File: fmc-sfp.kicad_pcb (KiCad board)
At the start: 2 copper layers, 89.5 x 70 mm, 35 parts, among them J1 ASP-134604-01, J2 SFP+, J3 SFP+, J4 132134, J5 132134, J6 132134, J7 132134, SW1 CHS-02TB, U1 MAX9113EKA_TT, U2 MAX9113EKA_TT

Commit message: clean up schematic and pcb
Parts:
- moved R10 0.52 mm to (71.0, 64.4)
- moved R9 0.52 mm to (71.0, 62.5)
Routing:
- net +3V3: track 122.4 -> 116.8 mm
- net GND: track 22.4 -> 25.1 mm, vias 10 -> 9
- net /lvds_0_rx_N: track 33.1 -> 34.9 mm
- net /lvds_1_tx_N: track 48.6 -> 50.2 mm
- net /lvds_0_tx_N: track 36.3 -> 35.1 mm
- net /FMC_LA02_N: track 5.20 -> 6.37 mm
- net /FMC_LA02_P: track 5.20 -> 6.35 mm
- net /lvds_0_tx_P: track 37.0 -> 37.7 mm
- net /lvds_1_tx_P: track 49.6 -> 50.3 mm
- net /lvds_0_rx_P: track 33.2 -> 32.6 mm

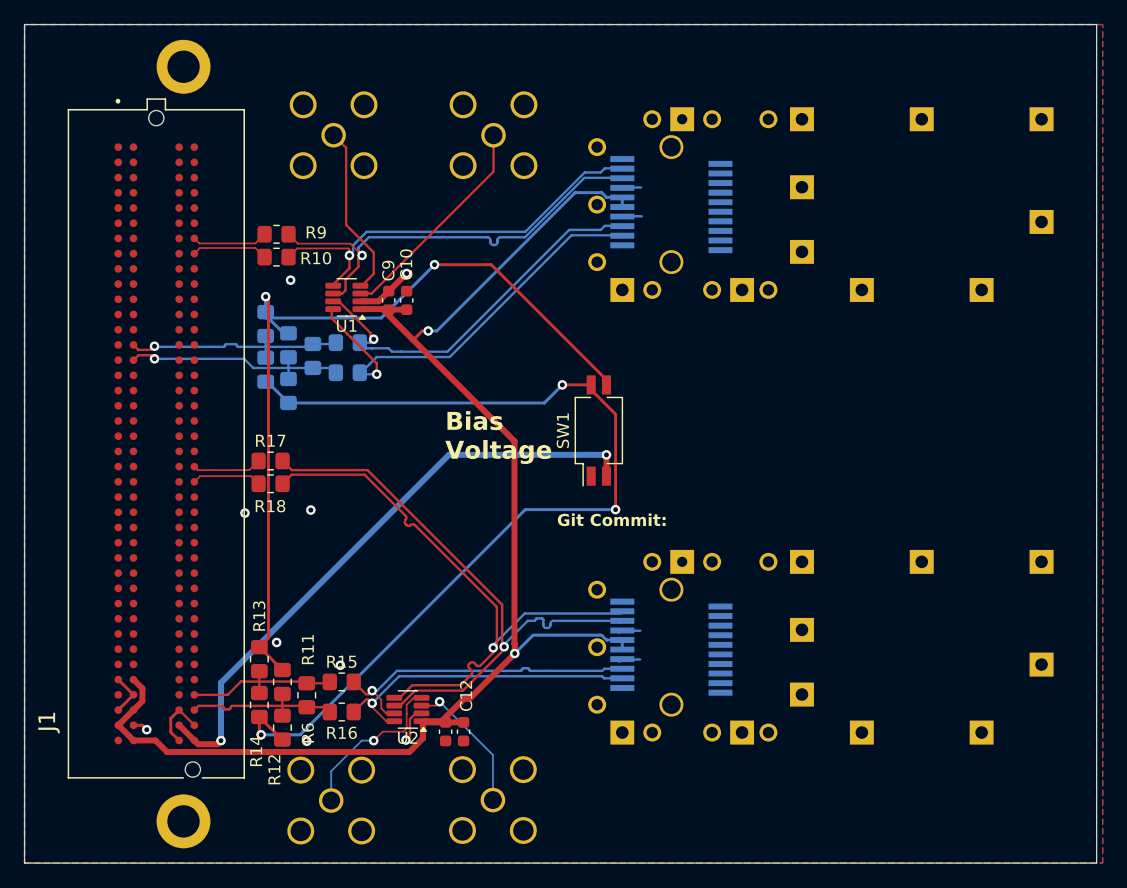
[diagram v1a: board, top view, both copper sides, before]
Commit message: make board more symetrical
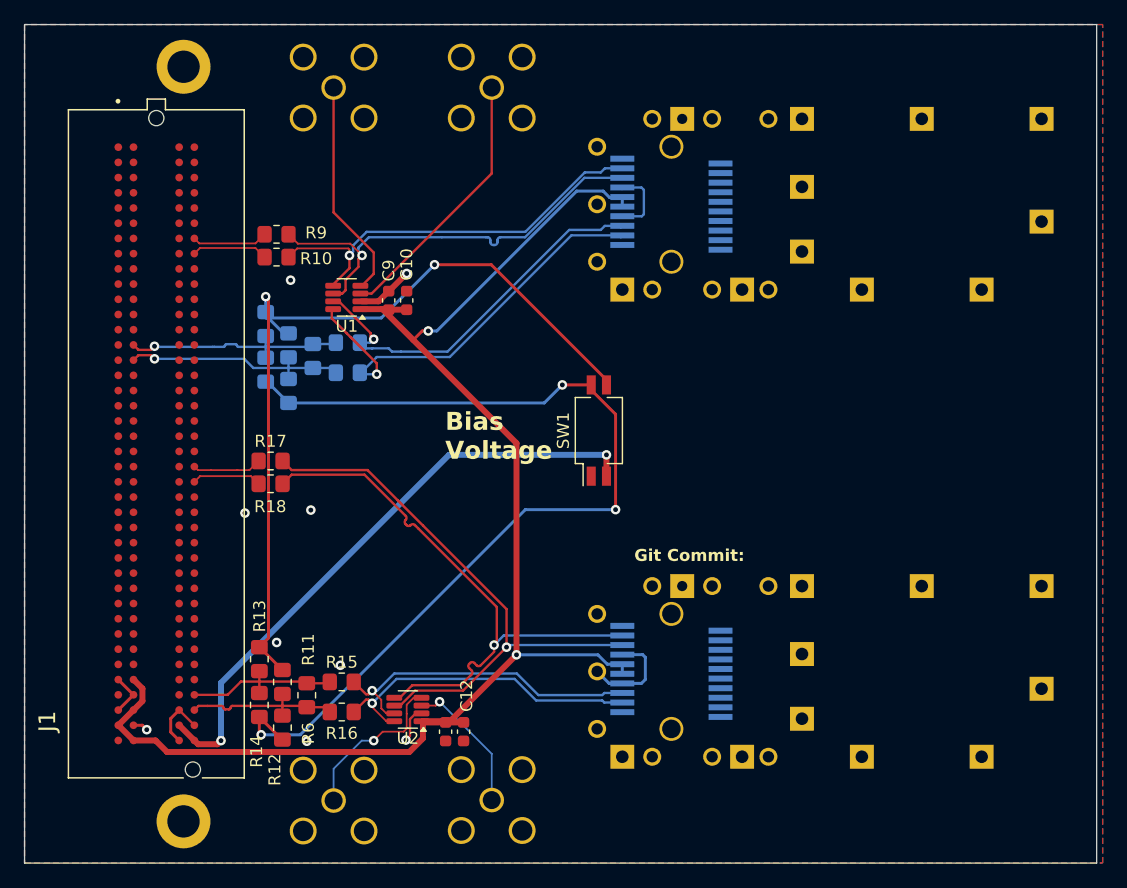
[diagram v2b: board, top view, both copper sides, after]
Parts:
- moved J4 3.98 mm to (89.0, 50.3)
- moved J5 3.98 mm to (75.8, 50.3)
- moved J2 2.02 mm to (97.8, 99.0)
- moved J6 0.20 mm to (75.8, 109.8)
- moved J7 0.10 mm to (89.0, 109.7)
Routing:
- net GND: track 25.1 -> 32.4 mm
- net /TX0: track 14.4 -> 18.3 mm
- net /RX0: track 18.2 -> 22.0 mm
- net /lvds_1_tx_P: track 50.3 -> 48.2 mm
- net /TX1: track 12.6 -> 13.6 mm
- net /lvds_1_tx_N: track 50.2 -> 49.3 mm
- net /lvds_1_rx_N: track 26.6 -> 27.3 mm

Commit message: add single x4 switch and test pads for differential probing
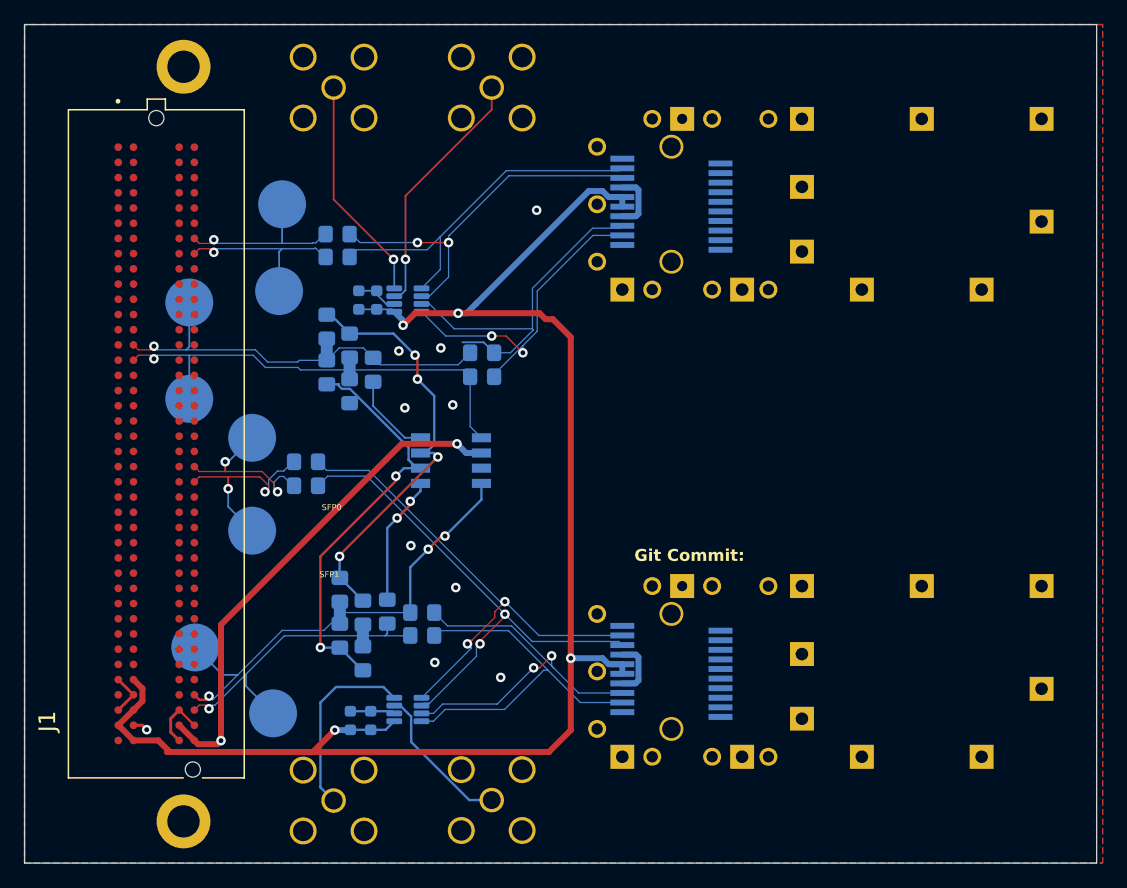
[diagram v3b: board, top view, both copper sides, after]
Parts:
- added TP1: SFP0 RX+, TestPoint:TestPoint_Pad_D4.0mm, B.Cu at (63.8, 68.2)
- added TP2: SFP0 RX-, TestPoint:TestPoint_Pad_D4.0mm, B.Cu at (63.8, 76.2)
- added TP3: SFP0 TX+, TestPoint:TestPoint_Pad_D4.0mm, B.Cu at (71.5, 60.0)
- added TP4: SFP0 TX-, TestPoint:TestPoint_Pad_D4.0mm, B.Cu at (71.2, 67.2)
- added TP5: SFP1 RX+, TestPoint:TestPoint_Pad_D4.0mm, B.Cu at (69.0, 79.5)
- added TP6: SFP1 RX-, TestPoint:TestPoint_Pad_D4.0mm, B.Cu at (69.0, 87.2)
- added TP7: SFP1 TX+, TestPoint:TestPoint_Pad_D4.0mm, B.Cu at (64.2, 97.0)
- added TP8: SFP1 TX-, TestPoint:TestPoint_Pad_D4.0mm, B.Cu at (70.8, 102.5)
- C10, C11, C12, C9, R10, R11, R12, R13, R14, R15, R16, R17, R18, R6, R9, U1, U2: moved to B.Cu
- SW1: value CHS-02TB -> SW_DIP_x04; footprint Button_Switch_SMD:SW_DIP_SPSTx02_Slide_Copal_CHS-02B_W7.62mm_P1.27mm -> Button_Switch_SMD:SW_DIP_SPSTx04_Slide_Copal_CHS-04A_W5.08mm_P1.27mm_JPin; moved to B.Cu
- moved SW1 12.6 mm to (85.6, 81.4), turned to 180 degrees
- moved R7 11.2 mm to (88.2, 72.4)
- moved R8 11.2 mm to (88.2, 74.4)
- moved R6 9.69 mm to (80.3, 94.0), turned to -90 degrees
- moved C12 9.50 mm to (77.2, 103.1), turned to 90 degrees
- moved R16 9.27 mm to (83.2, 96.0)
- moved R14 8.87 mm to (76.3, 96.0)
- moved R11 8.87 mm to (78.2, 94.1)
- moved R12 8.87 mm to (78.2, 97.9)
- moved R13 8.87 mm to (76.3, 92.2)
- moved R15 8.87 mm to (83.2, 94.1)
- moved C11 6.32 mm to (78.9, 103.1), turned to 90 degrees
- moved R1 5.16 mm to (79.1, 73.8)
- moved R2 5.10 mm to (75.2, 70.2)
- moved R3 5.10 mm to (75.2, 74.0)
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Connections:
- R1 pad 1: /FMC_LA09_N -> Net-(R1-Pad1)
- R6 pad 1: /FMC_LA32_N -> Net-(R6-Pad1)
- R6 pad 2: /FMC_LA32_P -> /FMC_LA32_N
- SW1 pad 1: GND -> /FMC_LA09_N
- SW1 pad 3: /bias_hi -> GND
- SW1 pad 4: /bias_lo -> /FMC_LA32_P
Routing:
- net /bias_lo: track 81.4 -> 35.3 mm, vias 3 -> 2
- net /bias_hi: track 70.4 -> 36.1 mm, vias 2 -> 4
- net /FMC_LA32_P: track 13.9 -> 41.2 mm, vias 0 -> 3
- net /FMC_LA09_N: track 19.5 -> 40.2 mm
- net /FMC_LA09_P: track 19.4 -> 36.3 mm
- net /FMC_LA32_N: track 13.7 -> 28.2 mm, vias 0 -> 1
- net +3V3: track 116.6 -> 129.4 mm, vias 2 -> 4
- net Net-(R6-Pad1): track 0.00 -> 10.9 mm, vias 0 -> 2
- net /FMC_LA19_N: track 5.82 -> 16.5 mm, vias 0 -> 2
- net /FMC_LA19_P: track 5.80 -> 15.1 mm, vias 0 -> 2
- net /FMC_LA02_N: track 6.37 -> 15.3 mm, vias 0 -> 1
- net VADJ: track 50.9 -> 42.3 mm
- net /FMC_LA02_P: track 6.35 -> 15.0 mm, vias 0 -> 1
- net Net-(R1-Pad1): track 0.00 -> 7.09 mm
- net /lvds_0_rx_N: track 34.9 -> 28.1 mm, vias 1 -> 2
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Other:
- board text added: "SW1: 1. Termination SFP0 2. Bias Voltage High 3. Bias Voltage Low 4. Termination SFP1"
- board text removed: "Bias Voltage"

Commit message: fix DRC issues
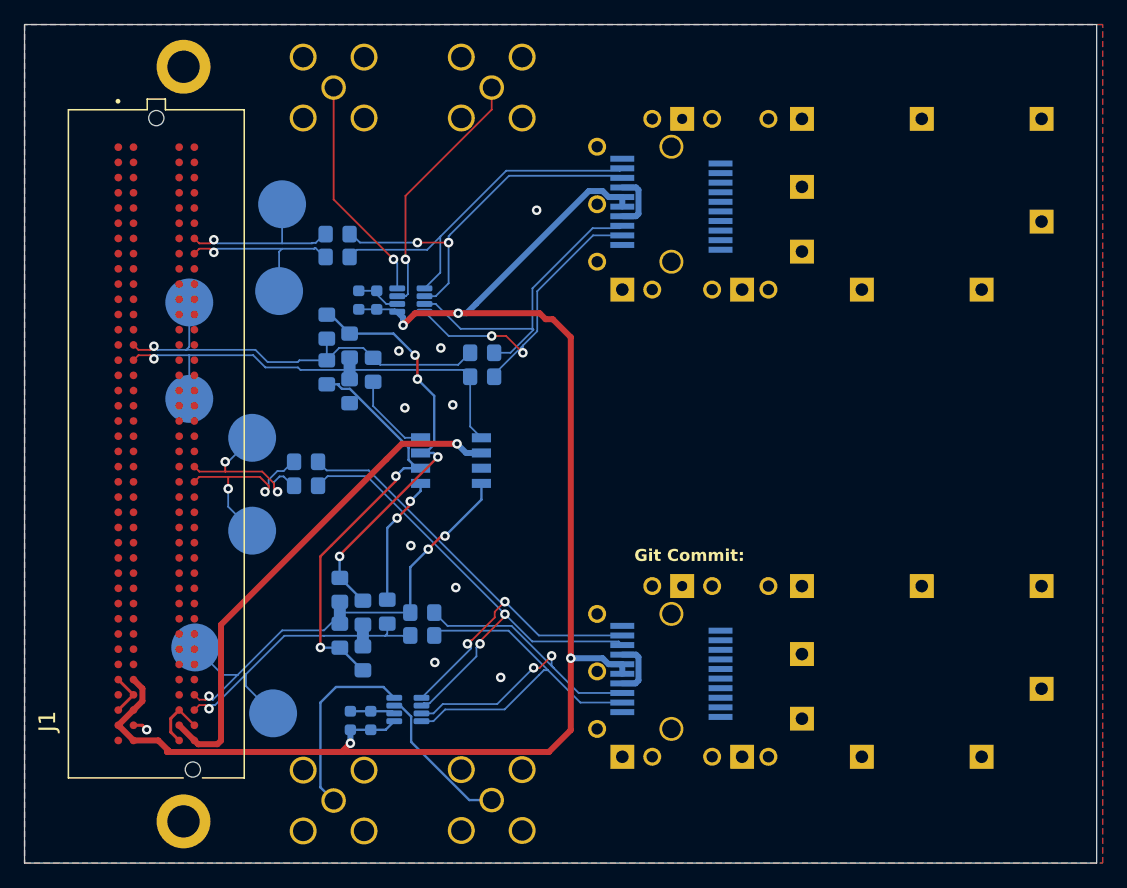
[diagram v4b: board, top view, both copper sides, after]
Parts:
- moved U1 0.25 mm to (82.2, 68.0)
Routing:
- net /lvds_0_rx_P: track 30.4 -> 27.1 mm
- net +3V3: track 129.4 -> 130.2 mm
- net VADJ: vias 2 -> 1
